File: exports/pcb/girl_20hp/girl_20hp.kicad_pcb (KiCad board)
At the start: 2 copper layers, 101.3 x 128.5 mm, 1 part

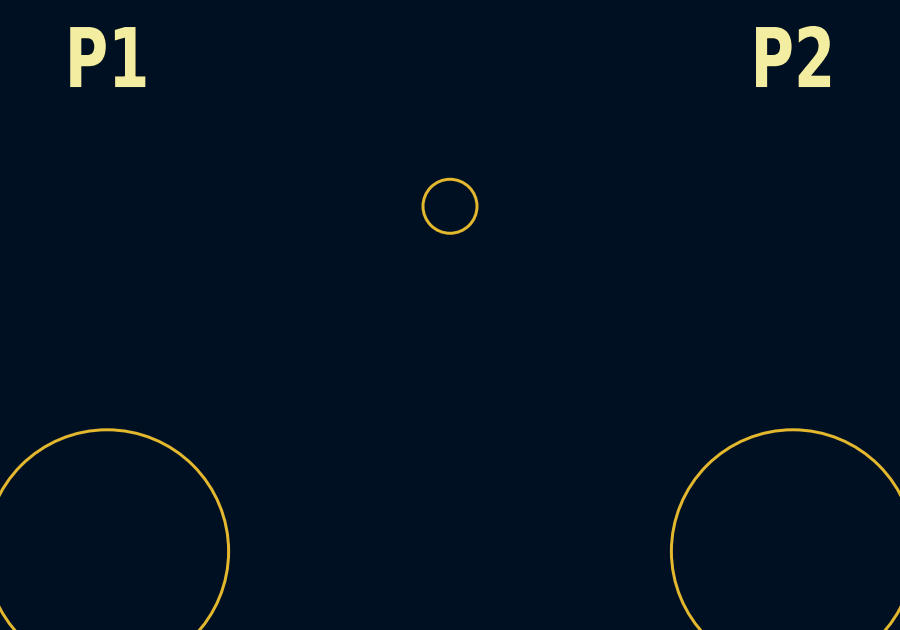
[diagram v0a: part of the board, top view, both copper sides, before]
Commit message: Girl: the pot dial scales, and the calibration hole named
Two things the first pass got wrong, both from the same mistake - filtering
sub-millimetre circles out of the plot as noise.

The 88 Ø1.2 circles are a dial scale printed around every pot: eleven dots 30
degrees apart on an r=8 circle, with the bottom 60 degrees left out, which is the
dead zone of a 300-degree pot. They are silkscreen, not holes - they appear on
the plot's silkscreen layer and nowhere else, where every real hole also shows on
the mask and drill layers. That is the test, and it is now written down.

The Ø1.7 hole I had flagged as "purpose unknown" is calibration access - a
screwdriver hole for a trimmer behind the panel. Labelled CAL. It is the one hole
under 2 mm that appears on every layer, which is what separates it from the dots.

Verified against the plot: 88 dots, 11 per pot, at exactly r=8.0 and the same
eleven angles.

The generator grew a SilkDot for this - a marking rather than a hole - and a
`dial` spec on a control that generates the ring. The preview draws them, so the
PNG still shows everything the gerbers carry.

Co-Authored-By: Claude Opus 5 (1M context) <noreply@anthropic.com>
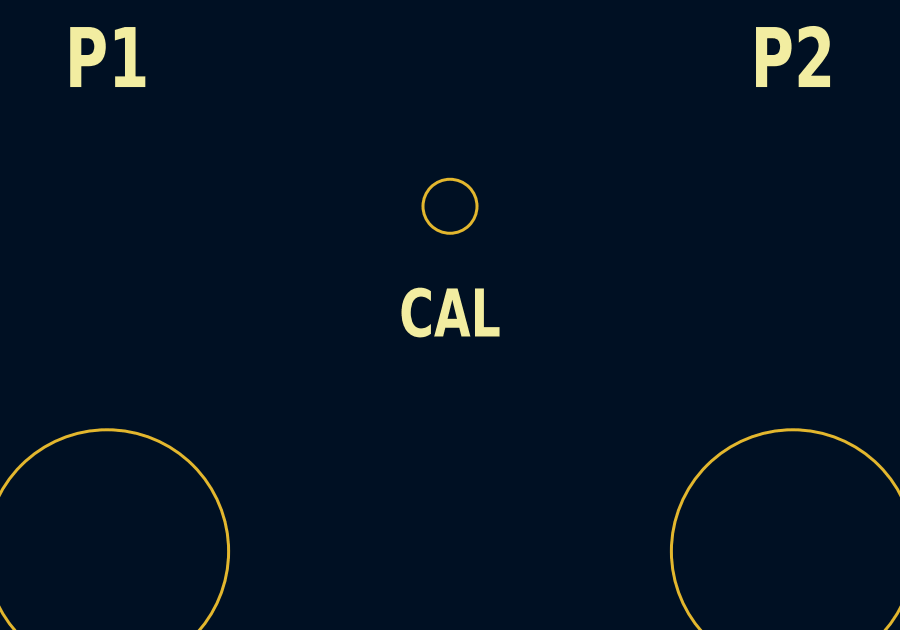
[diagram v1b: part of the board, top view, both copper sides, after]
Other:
- board text added: "CAL"

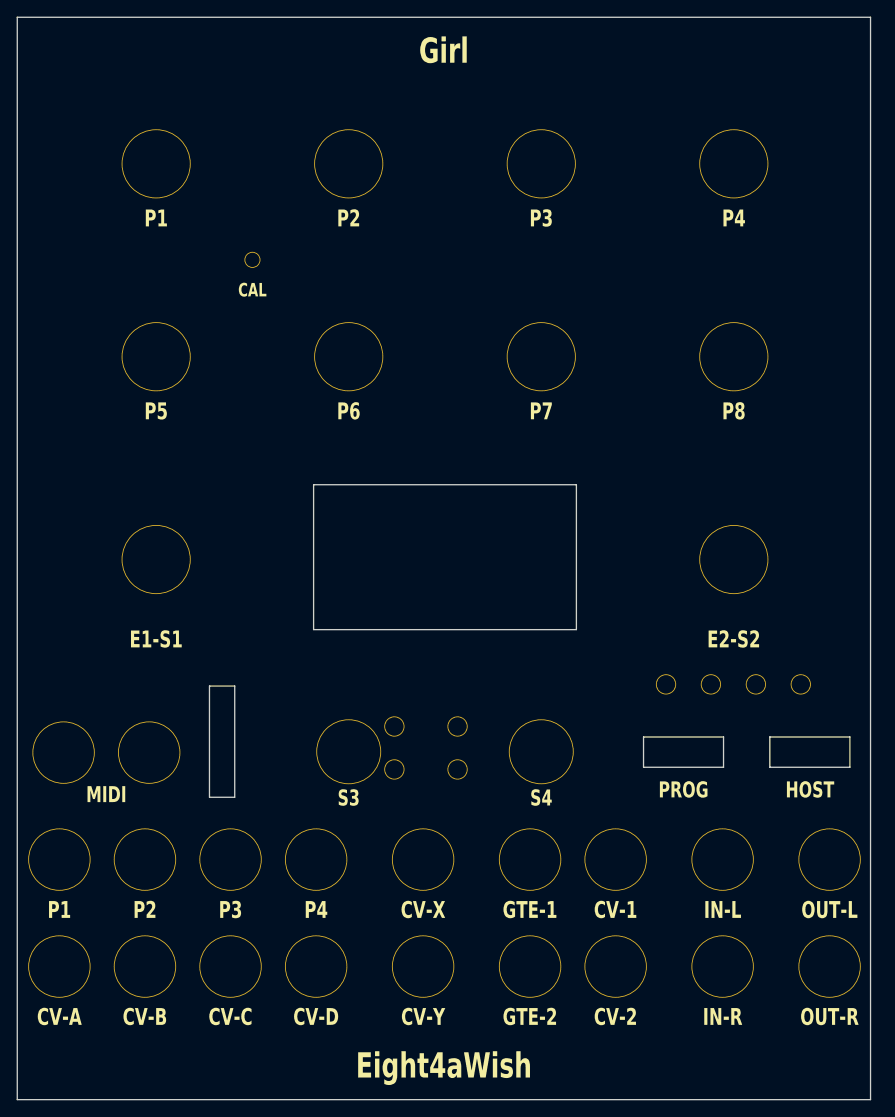
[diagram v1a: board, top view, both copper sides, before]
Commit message: Panels say what the module does, not what the board's pins are called
David's catch, and it applied to both boards.

girl_20hp reproduced the Big Genes' own pin names - P1..P8 on the pots, CV-A..D
on the jacks. That documents the board, not Girl. Relabelled from
eurorack_modules/docs/KSOLOTI_ELEMENTS.md: GEOM / BRIGHT / DAMP / POS on the
resonator row, BOW / BLOW / STRIKE / SPACE on the exciters, CONTOUR and ASSIGN on
the encoders with their push functions under them, PLAY and PAGE on the buttons.

And the thing behind the question: controls whose function changes with a page.
Girl's S4 cycles P5-P7 through level, meta and timbre - three sets, which is what
the dial scales around each pot are there to serve. Sorrow has the same problem
one page smaller: a short press on B7 turns X / Y / DENSITY / CHAOS into the
per-drum density trims plus wildness.

Sorrow's was the worse omission. The word missing from the panel was WILDNESS,
which is the control the module is named around, and there was an empty
HOLE_LABELS_ABOVE tuple sitting there the whole time waiting for it.

The generator grew stacked labels for this: `labels: [...]` prints the primary
name full size and each later page under it, smaller. Jacks carry the board's
name and Girl's use of it, because a Big Genes owner needs to find CV-A and a
Girl player needs to know it is Flow.

Gerbers regenerated for both. NOT ordered - see the preview before spending money.

Co-Authored-By: Claude Opus 5 (1M context) <noreply@anthropic.com>
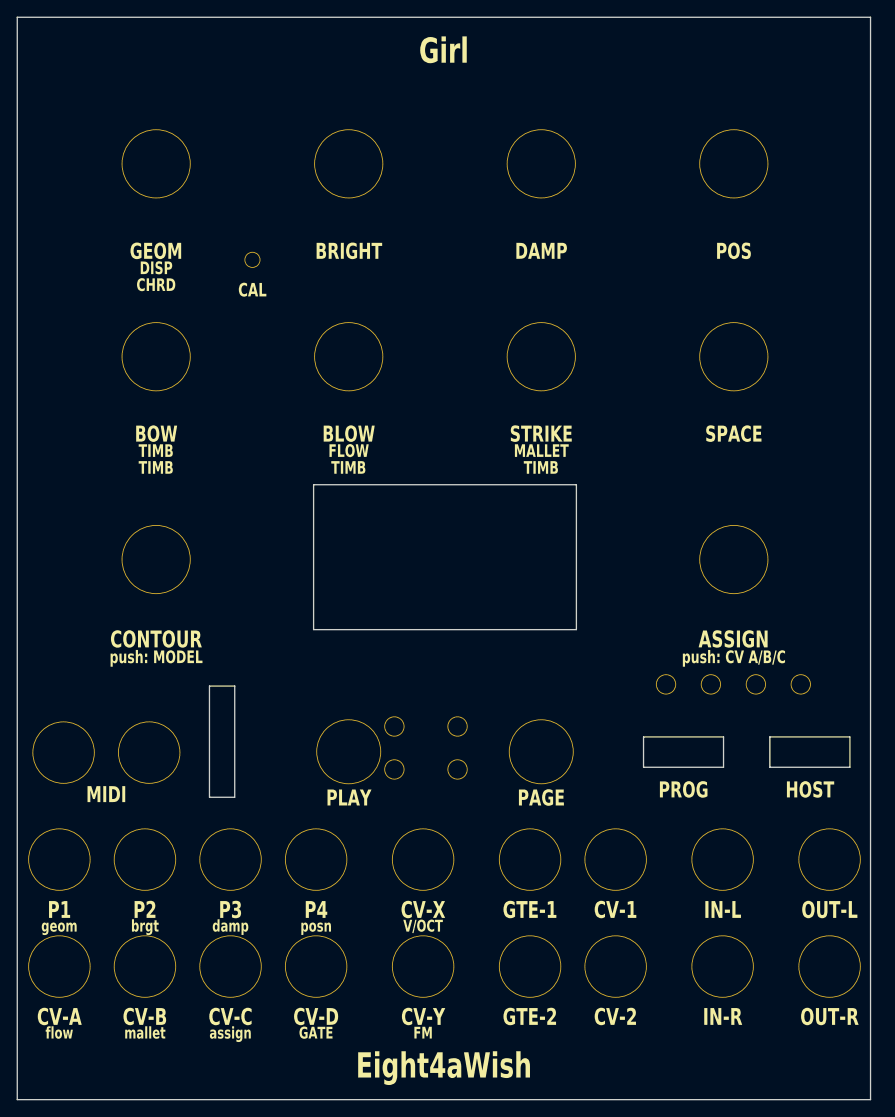
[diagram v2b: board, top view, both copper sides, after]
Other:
- board text added: "ASSIGN"
- board text added: "BLOW"
- board text added: "BOW"
- board text added: "BRIGHT"
- board text added: "CHRD"
- board text added: "CONTOUR"
- board text added: "DAMP"
- board text added: "DISP"
- board text added: "FLOW"
- board text added: "FM"
- board text added: "GATE"
- board text added: "GEOM"
- board text added: "MALLET"
- board text added: "PAGE"
- board text added: "PLAY"
- board text added: "POS"
- board text added: "SPACE"
- board text added: "STRIKE"
- board text added: "TIMB"
- board text added: "V/OCT"
- board text added: "assign"
- board text added: "brgt"
- board text added: "damp"
- board text added: "flow"
- board text added: "geom"
- board text added: "mallet"
- board text added: "posn"
- board text added: "push: CV A/B/C"
- board text added: "push: MODEL"
- board text removed: "E1-S1"
- board text removed: "E2-S2"
- board text removed: "P5"
- board text removed: "P6"
- board text removed: "P7"
- board text removed: "P8"
- board text removed: "S3"
- board text removed: "S4"
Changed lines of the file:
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@@
 		(stroke (width 0.1) (type solid)) (fill none)
 		(layer "Edge.Cuts"))
-	(gr_text "P1" (at 16.49 23.9) (layer "F.SilkS")
+	(gr_text "GEOM" (at 16.49 27.8) (layer "F.SilkS")
+		(effects (font (size 1.9 1.368) (thickness 0.323) bold))
+	)
+	(gr_text "DISP" (at 16.49 29.8) (layer "F.SilkS")
+		(effects (font (size 1.5 1.08) (thickness 0.255) bold))
+	)
+	(gr_text "CHRD" (at 16.49 31.8) (layer "F.SilkS")
+		(effects (font (size 1.5 1.08) (thickness 0.255) bold))
+	)
+	(gr_text "BRIGHT" (at 39.35 27.8) (layer "F.SilkS")
+		(effects (font (size 1.9 1.368) (thickness 0.323) bold))
+	)
+	(gr_text "DAMP" (at 62.21 27.8) (layer "F.SilkS")
+		(effects (font (size 1.9 1.368) (thickness 0.323) bold))
+	)
+	(gr_text "POS" (at 85.07 27.8) (layer "F.SilkS")
+		(effects (font (size 1.9 1.368) (thickness 0.323) bold))
+	)
+	(gr_text "BOW" (at 16.49 49.5) (layer "F.SilkS")
+		(effects (font (size 1.9 1.368) (thickness 0.323) bold))
+	)
+	(gr_text "TIMB" (at 16.49 51.5) (layer "F.SilkS")
+		(effects (font (size 1.5 1.08) (thickness 0.255) bold))
+	)
+	(gr_text "TIMB" (at 16.49 53.5) (layer "F.SilkS")
+		(effects (font (size 1.5 1.08) (thickness 0.255) bold))
+	)
+	(gr_text "BLOW" (at 39.35 49.5) (layer "F.SilkS")
+		(effects (font (size 1.9 1.368) (thickness 0.323) bold))
+	)
+	(gr_text "FLOW" (at 39.35 51.5) (layer "F.SilkS")
+		(effects (font (size 1.5 1.08) (thickness 0.255) bold))
+	)
+	(gr_text "TIMB" (at 39.35 53.5) (layer "F.SilkS")
+		(effects (font (size 1.5 1.08) (thickness 0.255) bold))
+	)
+	(gr_text "STRIKE" (at 62.21 49.5) (layer "F.SilkS")
+		(effects (font (size 1.9 1.368) (thickness 0.323) bold))
+	)
+	(gr_text "MALLET" (at 62.21 51.5) (layer "F.SilkS")
+		(effects (font (size 1.5 1.08) (thickness 0.255) bold))
+	)
+	(gr_text "TIMB" (at 62.21 53.5) (layer "F.SilkS")
+		(effects (font (size 1.5 1.08) (thickness 0.255) bold))
+	)
+	(gr_text "SPACE" (at 85.07 49.5) (layer "F.SilkS")
+		(effects (font (size 1.9 1.368) (thickness 0.323) bold))
+	)
+	(gr_text "CONTOUR" (at 16.49 73.88) (layer "F.SilkS")
 		(effects (font (size 2 1.44) (thickness 0.34) bold))
 	)
-	(gr_text "P2" (at 39.35 23.9) (layer "F.SilkS")
+	(gr_text "push: MODEL" (at 16.49 75.98) (layer "F.SilkS")
+		(effects (font (size 1.5 1.08) (thickness 0.255) bold))
+	)
+	(gr_text "ASSIGN" (at 85.07 73.88) (layer "F.SilkS")
 		(effects (font (size 2 1.44) (thickness 0.34) bold))
 	)
-	(gr_text "P3" (at 62.21 23.9) (layer "F.SilkS")
-		(effects (font (size 2 1.44) (thickness 0.34) bold))
-	)
-	(gr_text "P4" (at 85.07 23.9) (layer "F.SilkS")
-		(effects (font (size 2 1.44) (thickness 0.34) bold))
-	)
-	(gr_text "P5" (at 16.49 46.8) (layer "F.SilkS")
-		(effects (font (size 2 1.44) (thickness 0.34) bold))
-	)
-	(gr_text "P6" (at 39.35 46.8) (layer "F.SilkS")
-		(effects (font (size 2 1.44) (thickness 0.34) bold))
-	)
-	(gr_text "P7" (at 62.21 46.8) (layer "F.SilkS")
-		(effects (font (size 2 1.44) (thickness 0.34) bold))
-	)
-	(gr_text "P8" (at 85.07 46.8) (layer "F.SilkS")
-		(effects (font (size 2 1.44) (thickness 0.34) bold))
-	)
-	(gr_text "E1-S1" (at 16.49 73.88) (layer "F.SilkS")
-		(effects (font (size 2 1.44) (thickness 0.34) bold))
-	)
-	(gr_text "E2-S2" (at 85.07 73.88) (layer "F.SilkS")
-		(effects (font (size 2 1.44) (thickness 0.34) bold))
+	(gr_text "push: CV A/B/C" (at 85.07 75.98) (layer "F.SilkS")
+		(effects (font (size 1.5 1.08) (thickness 0.255) bold))
 	)
 	(gr_text "MIDI" (at 10.58 92.3) (layer "F.SilkS")
 		(effects (font (size 1.9 1.368) (thickness 0.323) bold))
 	)
-	(gr_text "S3" (at 39.35 92.7) (layer "F.SilkS")
+	(gr_text "PLAY" (at 39.35 92.7) (layer "F.SilkS")
 		(effects (font (size 1.9 1.368) (thickness 0.323) bold))
 	)
-	(gr_text "S4" (at 62.21 92.7) (layer "F.SilkS")
+	(gr_text "PAGE" (at 62.21 92.7) (layer "F.SilkS")
 		(effects (font (size 1.9 1.368) (thickness 0.323) bold))
 	)
@@
 		(effects (font (size 2 1.44) (thickness 0.34) bold))
 	)
+	(gr_text "geom" (at 5 107.9) (layer "F.SilkS")
+		(effects (font (size 1.4 1.008) (thickness 0.238) bold))
+	)
 	(gr_text "P2" (at 15.16 106) (layer "F.SilkS")
 		(effects (font (size 2 1.44) (thickness 0.34) bold))
+	)
+	(gr_text "brgt" (at 15.16 107.9) (layer "F.SilkS")
+		(effects (font (size 1.4 1.008) (thickness 0.238) bold))
 	)
 	(gr_text "P3" (at 25.32 106) (layer "F.SilkS")
 		(effects (font (size 2 1.44) (thickness 0.34) bold))
 	)
+	(gr_text "damp" (at 25.32 107.9) (layer "F.SilkS")
+		(effects (font (size 1.4 1.008) (thickness 0.238) bold))
+	)
 	(gr_text "P4" (at 35.48 106) (layer "F.SilkS")
 		(effects (font (size 2 1.44) (thickness 0.34) bold))
 	)
+	(gr_text "posn" (at 35.48 107.9) (layer "F.SilkS")
+		(effects (font (size 1.4 1.008) (thickness 0.238) bold))
+	)
 	(gr_text "CV-X" (at 48.18 106) (layer "F.SilkS")
 		(effects (font (size 2 1.44) (thickness 0.34) bold))
+	)
+	(gr_text "V/OCT" (at 48.18 107.9) (layer "F.SilkS")
+		(effects (font (size 1.4 1.008) (thickness 0.238) bold))
 	)
 	(gr_text "GTE-1" (at 60.88 106) (layer "F.SilkS")
@@
 		(effects (font (size 2 1.44) (thickness 0.34) bold))
 	)
+	(gr_text "flow" (at 5 120.6) (layer "F.SilkS")
+		(effects (font (size 1.4 1.008) (thickness 0.238) bold))
+	)
 	(gr_text "CV-B" (at 15.16 118.7) (layer "F.SilkS")
 		(effects (font (size 2 1.44) (thickness 0.34) bold))
+	)
+	(gr_text "mallet" (at 15.16 120.6) (layer "F.SilkS")
+		(effects (font (size 1.4 1.008) (thickness 0.238) bold))
 	)
 	(gr_text "CV-C" (at 25.32 118.7) (layer "F.SilkS")
 		(effects (font (size 2 1.44) (thickness 0.34) bold))
 	)
+	(gr_text "assign" (at 25.32 120.6) (layer "F.SilkS")
+		(effects (font (size 1.4 1.008) (thickness 0.238) bold))
+	)
 	(gr_text "CV-D" (at 35.48 118.7) (layer "F.SilkS")
 		(effects (font (size 2 1.44) (thickness 0.34) bold))
+	)
+	(gr_text "GATE" (at 35.48 120.6) (layer "F.SilkS")
+		(effects (font (size 1.4 1.008) (thickness 0.238) bold))
 	)
 	(gr_text "CV-Y" (at 48.18 118.7) (layer "F.SilkS")
 		(effects (font (size 2 1.44) (thickness 0.34) bold))
 	)
+	(gr_text "FM" (at 48.18 120.6) (layer "F.SilkS")
+		(effects (font (size 1.4 1.008) (thickness 0.238) bold))
+	)
 	(gr_text "GTE-2" (at 60.88 118.7) (layer "F.SilkS")

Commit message: Panels: David's pass on both
Sorrow
  The Home name now sits ABOVE the pot and the Kit name below it, one size
  smaller: DENS-KC, DENS-SN, DENS-HT, WILD. Brackets gone - the size difference
  does that job without punctuation.

  The generator grew LABELS_SECONDARY for it: a tuple of label texts that render
  at 78% of the label size, so a panel can carry a control's second function
  without it reading as a second control.

Girl
  Dial rings gone. CAL label gone - the HOLE stays, because a trimmer behind the
  panel is unreachable without it, and it is easy to put the word back.

  Resonator row is GEOM / BRGT / DAMP / POSN, one name each. P1's model variants
  (DISP, CHRD) come off the panel; the OLED already shows which model is live.

  Jacks: fixed functions say what they do - GEOM, BRGT, DAMP, POSN, V/OCT, FM,
  GATE. Assignable ones keep their board names, CV-A/B/C, because their function
  is whatever E2 last set it to. Everything Girl does not use loses its label:
  MIDI, GTE-1/2, CV-1/2, IN-L/R, HOST.

Both now use the same 2.6 mm labels and 3.0 mm branding as joy_10hp, which they
did not before - Girl was carrying per-control sizes between 1.4 and 2.0. Taking
the dial rings off freed the room for it.

Co-Authored-By: Claude Opus 5 (1M context) <noreply@anthropic.com>
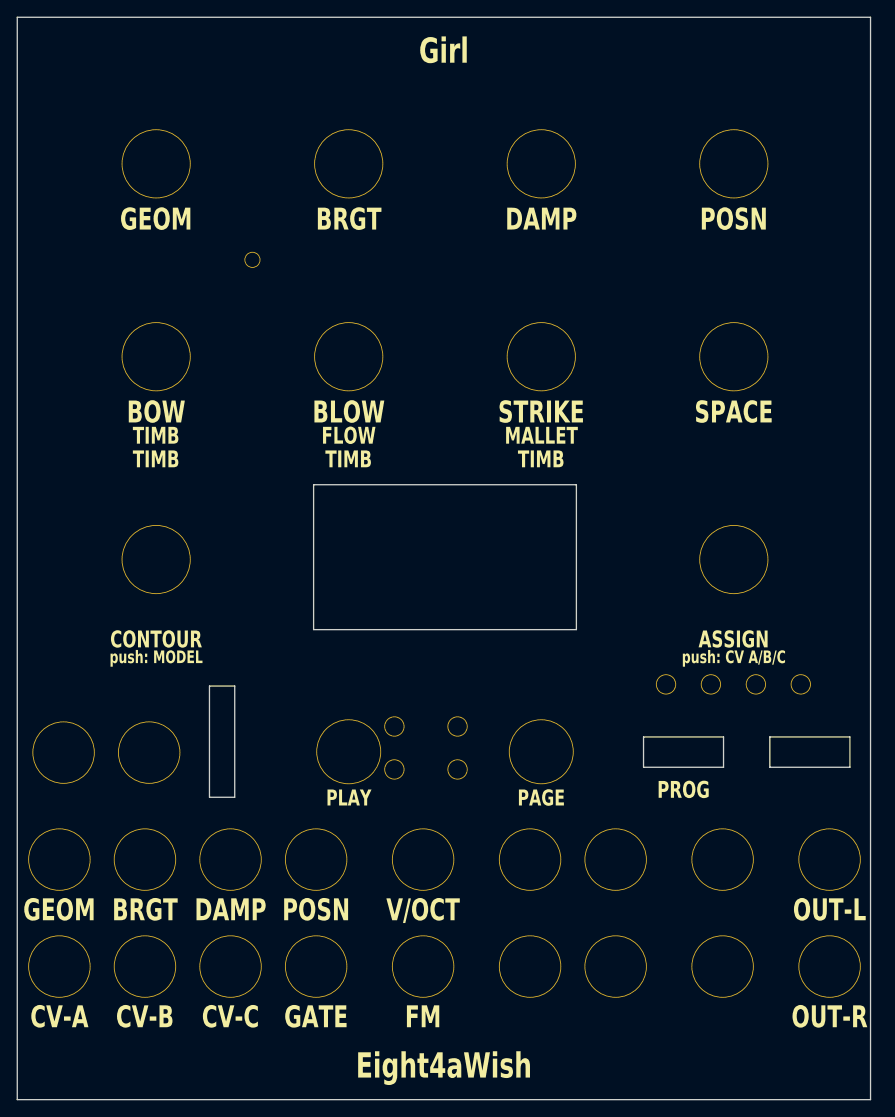
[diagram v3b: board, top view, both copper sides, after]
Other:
- board text added: "BRGT"
- board text added: "POSN"
- board text removed: "BRIGHT"
- board text removed: "CAL"
- board text removed: "CHRD"
- board text removed: "CV-1"
- board text removed: "CV-2"
- board text removed: "CV-D"
- board text removed: "CV-X"
- board text removed: "CV-Y"
- board text removed: "DISP"
- board text removed: "GTE-1"
- board text removed: "GTE-2"
- board text removed: "HOST"
- board text removed: "IN-L"
- board text removed: "IN-R"
- board text removed: "MIDI"
- board text removed: "P1"
- board text removed: "P2"
- board text removed: "P3"
- board text removed: "P4"
- board text removed: "POS"
- board text removed: "assign"
- board text removed: "brgt"
- board text removed: "damp"
- board text removed: "flow"
- board text removed: "geom"
- board text removed: "mallet"
- board text removed: "posn"
